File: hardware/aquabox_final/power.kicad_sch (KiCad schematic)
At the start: 0 parts

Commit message: Atualização
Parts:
- added J2: AC 220V, symbol Connector:Screw_Terminal_01x04
- added PS1: MC00100, MC00100:CONV_MC00100, symbol MC00100:MC00100
- added RV1: MOV-14D471K, symbol Device:Varistor
- added U1: HLK-10M05, Converter_ACDC:Converter_ACDC_Hi-Link_HLK-10Mxx, symbol Converter_ACDC:HLK-10M05
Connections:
- new net: J2.1 (Pin_1), J2.2 (Pin_2), RV1.1, U1.1 (AC/L)
- new net: J2.3 (Pin_3), J2.4 (Pin_4), RV1.2, U1.2 (AC/N)
- new net: PS1.IN-, U1.3 (-Vout)
- new net +3.3V: PS1.OUT+
- new net +5V: PS1.IN+, U1.4 (+Vout)
- new net GND: PS1.MH1 (MOUTING), PS1.MH2 (MOUTING), PS1.OUT-
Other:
- note added: "AC_L_IN"
- note added: "AC_L_OUT"
- note added: "AC_N_IN"
- note added: "AC_N_OUT"

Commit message: Desenvolvimento da fonte de alimentação.
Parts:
- added C1: 0.1uFx275V, symbol Device:C
- added C2: 220uF, symbol Device:C_Polarized
- added D1: RED, symbol Device:LED
- added F1: 1A 250V, symbol Device:Fuse
- added R1: 1M, symbol Device:R
- added R2: 4K7, symbol Device:R
- RV1: value MOV-14D471K -> 10D561K
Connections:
- net +5V: now also C2.1, R2.1
- net GND: now also PS1.IN-, U1.3 (-Vout), C2.2, D1.1 (K); no longer PS1.MH2 (MOUTING)
- net at RV1.1, U1.1 (AC/L): now also C1.1, F1.2, R1.1; no longer J2.1 (Pin_1), J2.2 (Pin_2)
- net NEUTRO: now reaches J2.3 (Pin_3), RV1.2, U1.2 (AC/N)
- net NEUTRO: now also C1.2, R1.2; no longer J2.4 (Pin_4)
- new net: D1.2 (A), R2.2
- new net PHASE: F1.1, J2.4 (Pin_4)
- new net R-C: J2.2 (Pin_2)
- new net R-NO: J2.1 (Pin_1)
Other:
- note removed: "AC_L_IN"
- note removed: "AC_L_OUT"
- note removed: "AC_N_IN"
- note removed: "AC_N_OUT"
- moved on the sheet: J2, PS1, RV1, U1

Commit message: Atualização
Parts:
- R2: value 4K7 -> 220R
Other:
- company: (none) -> INVENCTUS - Soluções Tecnológicas
- title: (none) -> Power
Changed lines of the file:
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@@
 	(generator_version "10.0")
 	(paper "A4")
+	(title_block
+		(title "Power")
+		(date "2026-06-02")
+		(rev "1.0.0")
+		(company "INVENCTUS - Soluções Tecnológicas")
+		(comment 1 "Eng. José Adriano")
+	)
 	(junction
 		(at 190.5 86.36)
@@
 	(wire
 		(pts
-			(xy 59.69 93.98) (xy 63.5 93.98)
-		)
-		(stroke
-			(width 0)
-			(type default)
-		)
-	)
-	(wire
-		(pts
 			(xy 123.19 101.6) (xy 123.19 105.41)
 		)
@@
 	(wire
 		(pts
+			(xy 59.69 96.52) (xy 62.23 96.52)
+		)
+		(stroke
+			(width 0)
+			(type default)
+		)
+	)
+	(wire
+		(pts
 			(xy 234.95 99.06) (xy 234.95 110.49)
 		)
@@
 	(wire
 		(pts
+			(xy 59.69 93.98) (xy 62.23 93.98)
+		)
+		(stroke
+			(width 0)
+			(type default)
+		)
+	)
+	(wire
+		(pts
 			(xy 123.19 90.17) (xy 123.19 93.98)
 		)
@@
 	(wire
 		(pts
-			(xy 59.69 96.52) (xy 63.5 96.52)
-		)
-		(stroke
-			(width 0)
-			(type default)
-		)
-	)
-	(wire
-		(pts
 			(xy 190.5 93.98) (xy 190.5 97.79)
 		)
@@
 			(width 0)
 			(type default)
+		)
+	)
+	(global_label "R-C"
+		(shape input)
+		(at 62.23 96.52 0)
+		(fields_autoplaced yes)
+		(effects
+			(font
+				(size 1.27 1.27)
+			)
+			(justify left)
+		)
+		(property "Intersheetrefs" "${INTERSHEET_REFS}"
+			(at 69.3276 96.52 0)
+			(hide yes)
+			(show_name no)
+			(do_not_autoplace no)
+			(effects
+				(font
+					(size 1.27 1.27)
+				)
+				(justify left)
+			)
 		)
 	)
@@
 		)
 	)
-	(hierarchical_label "R-C"
+	(global_label "R-NO"
 		(shape input)
-		(at 63.5 96.52 0)
+		(at 62.23 93.98 0)
+		(fields_autoplaced yes)
 		(effects
 			(font
@@
 			(justify left)
 		)
-	)
-	(hierarchical_label "R-NO"
-		(shape input)
-		(at 63.5 93.98 0)
-		(effects
-			(font
-				(size 1.27 1.27)
-			)
-			(justify left)
+		(property "Intersheetrefs" "${INTERSHEET_REFS}"
+			(at 70.7186 93.98 0)
+			(hide yes)
+			(show_name no)
+			(do_not_autoplace no)
+			(effects
+				(font
+					(size 1.27 1.27)
+				)
+				(justify left)
+			)
 		)
 	)
@@
 			)
 		)
-		(property "Value" "4K7"
+		(property "Value" "220R"
 			(at 193.04 91.4399 0)
 			(show_name no)

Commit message: Atualização
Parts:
- added J6: Entrada de 12V, symbol Connector:Screw_Terminal_01x02
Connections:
- new net +12V: J6.2 (Pin_2)
- new net GND1: J6.1 (Pin_1)

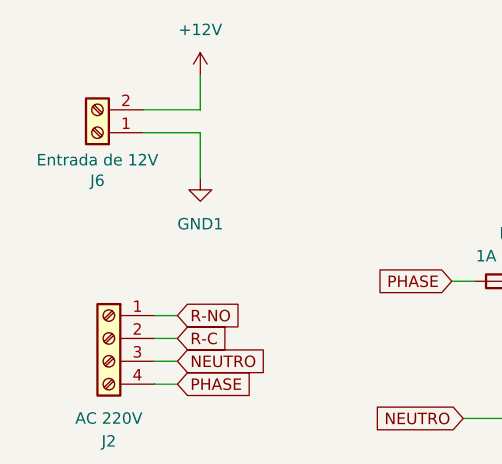
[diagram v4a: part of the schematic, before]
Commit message: Acionamento da bom e solenóides
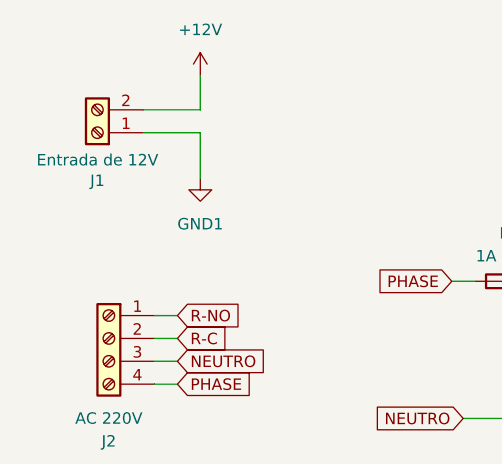
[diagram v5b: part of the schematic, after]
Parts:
- renumbered J6 to J1
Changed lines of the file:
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@@
 		(dnp no)
 		(fields_autoplaced yes)
-		(property "Reference" "#PWR03"
+		(property "Reference" "#PWR06"
 			(at 234.95 86.36 0)
 			(hide yes)
@@
 			(project "aquabox_final"
 				(path "/c895ac8d-c639-4fea-ba83-739985d9c75e/44a7b396-f10f-46a5-80f2-f6866e22a5c3"
-					(reference "#PWR03")
+					(reference "#PWR06")
 					(unit 1)
 				)
@@
 		(dnp no)
 		(fields_autoplaced yes)
-		(property "Reference" "#PWR035"
+		(property "Reference" "#PWR02"
 			(at 64.77 85.09 0)
 			(hide yes)
@@
 			(project "aquabox_final"
 				(path "/c895ac8d-c639-4fea-ba83-739985d9c75e/44a7b396-f10f-46a5-80f2-f6866e22a5c3"
-					(reference "#PWR035")
+					(reference "#PWR02")
 					(unit 1)
 				)
@@
 		(dnp no)
 		(fields_autoplaced yes)
-		(property "Reference" "#PWR036"
+		(property "Reference" "#PWR01"
 			(at 64.77 71.12 0)
 			(hide yes)
@@
 			(project "aquabox_final"
 				(path "/c895ac8d-c639-4fea-ba83-739985d9c75e/44a7b396-f10f-46a5-80f2-f6866e22a5c3"
-					(reference "#PWR036")
+					(reference "#PWR01")
 					(unit 1)
 				)
@@
 		(dnp no)
 		(fields_autoplaced yes)
-		(property "Reference" "#PWR01"
+		(property "Reference" "#PWR05"
 			(at 215.9 116.84 0)
 			(hide yes)
@@
 			(project "aquabox_final"
 				(path "/c895ac8d-c639-4fea-ba83-739985d9c75e/44a7b396-f10f-46a5-80f2-f6866e22a5c3"
-					(reference "#PWR01")
+					(reference "#PWR05")
 					(unit 1)
 				)
@@
 		(dnp no)
 		(fields_autoplaced yes)
-		(property "Reference" "#PWR04"
+		(property "Reference" "#PWR07"
 			(at 234.95 116.84 0)
 			(hide yes)
@@
 			(project "aquabox_final"
 				(path "/c895ac8d-c639-4fea-ba83-739985d9c75e/44a7b396-f10f-46a5-80f2-f6866e22a5c3"
-					(reference "#PWR04")
+					(reference "#PWR07")
 					(unit 1)
 				)
@@
 		(dnp no)
 		(fields_autoplaced yes)
-		(property "Reference" "#PWR05"
+		(property "Reference" "#PWR04"
 			(at 190.5 116.84 0)
 			(hide yes)
@@
 			(project "aquabox_final"
 				(path "/c895ac8d-c639-4fea-ba83-739985d9c75e/44a7b396-f10f-46a5-80f2-f6866e22a5c3"
-					(reference "#PWR05")
+					(reference "#PWR04")
 					(unit 1)
 				)
@@
 		(dnp no)
 		(fields_autoplaced yes)
-		(property "Reference" "#PWR02"
+		(property "Reference" "#PWR03"
 			(at 190.5 86.36 0)
 			(hide yes)
@@
 			(project "aquabox_final"
 				(path "/c895ac8d-c639-4fea-ba83-739985d9c75e/44a7b396-f10f-46a5-80f2-f6866e22a5c3"
-					(reference "#PWR02")
+					(reference "#PWR03")
 					(unit 1)
 				)
@@
 		(in_pos_files yes)
 		(dnp no)
-		(property "Reference" "J6"
+		(property "Reference" "J1"
 			(at 53.34 78.994 0)
 			(show_name no)
@@
 			(project "aquabox_final"
 				(path "/c895ac8d-c639-4fea-ba83-739985d9c75e/44a7b396-f10f-46a5-80f2-f6866e22a5c3"
-					(reference "J6")
-					(unit 1)
-				)
+					(reference "J1")
+					(unit 1)
+				)

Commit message: Atualização
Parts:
- added D11: RED, symbol Device:LED
- added R45: 1K, symbol Device:R
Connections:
- net +12V: now also J1.1 (Pin_1), R45.1; no longer J1.2 (Pin_2)
- net GND1: now also J1.2 (Pin_2), D11.1 (K); no longer J1.1 (Pin_1)
- new net: D11.2 (A), R45.2
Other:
- moved on the sheet: J1

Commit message: Implementação do RTC
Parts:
- renumbered D11 to D1, D1 to D2, R45 to R1, R1 to R2, R2 to R3
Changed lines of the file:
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@@
 		(dnp no)
 		(fields_autoplaced yes)
-		(property "Reference" "R1"
+		(property "Reference" "R2"
 			(at 142.24 96.5199 0)
 			(show_name no)
@@
 			(project "aquabox_final"
 				(path "/c895ac8d-c639-4fea-ba83-739985d9c75e/44a7b396-f10f-46a5-80f2-f6866e22a5c3"
-					(reference "R1")
+					(reference "R2")
 					(unit 1)
 				)
@@
 		(dnp no)
 		(fields_autoplaced yes)
-		(property "Reference" "R2"
+		(property "Reference" "R3"
 			(at 193.04 88.8999 0)
 			(show_name no)
@@
 			(project "aquabox_final"
 				(path "/c895ac8d-c639-4fea-ba83-739985d9c75e/44a7b396-f10f-46a5-80f2-f6866e22a5c3"
-					(reference "R2")
+					(reference "R3")
 					(unit 1)
 				)
@@
 		(dnp no)
 		(fields_autoplaced yes)
-		(property "Reference" "R45"
+		(property "Reference" "R1"
 			(at 72.39 49.5299 0)
 			(show_name no)
@@
 			(project "aquabox_final"
 				(path "/c895ac8d-c639-4fea-ba83-739985d9c75e/44a7b396-f10f-46a5-80f2-f6866e22a5c3"
-					(reference "R45")
+					(reference "R1")
 					(unit 1)
 				)
@@
 		(dnp no)
 		(fields_autoplaced yes)
-		(property "Reference" "D1"
+		(property "Reference" "D2"
 			(at 194.31 101.9174 90)
 			(show_name no)
@@
 			(project "aquabox_final"
 				(path "/c895ac8d-c639-4fea-ba83-739985d9c75e/44a7b396-f10f-46a5-80f2-f6866e22a5c3"
-					(reference "D1")
+					(reference "D2")
 					(unit 1)
 				)
@@
 		(dnp no)
 		(fields_autoplaced yes)
-		(property "Reference" "D11"
+		(property "Reference" "D1"
 			(at 73.66 61.2774 90)
 			(show_name no)
@@
 			(project "aquabox_final"
 				(path "/c895ac8d-c639-4fea-ba83-739985d9c75e/44a7b396-f10f-46a5-80f2-f6866e22a5c3"
-					(reference "D11")
-					(unit 1)
-				)
+					(reference "D1")
+					(unit 1)
+				)
